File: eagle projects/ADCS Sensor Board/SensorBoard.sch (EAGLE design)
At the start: 113 parts, among them J1 HDR_10_EZFET_DEBUGGER, J3 HDR_2X5_GRPB052VWQS-RC, Q1 PMV16XN, Q2 IRLML6246TRPBF, Q3 IRLML2246TRPBF, U1 MSP430F5529IPN, U2 LMV321, U3 ADS7841E_2K5, U4 LMV321, U5 LMV321, U7 HMC1053, Y1 32.768kHz, Y2 CSTCR4M00G15L99, Y3 32.768kHz

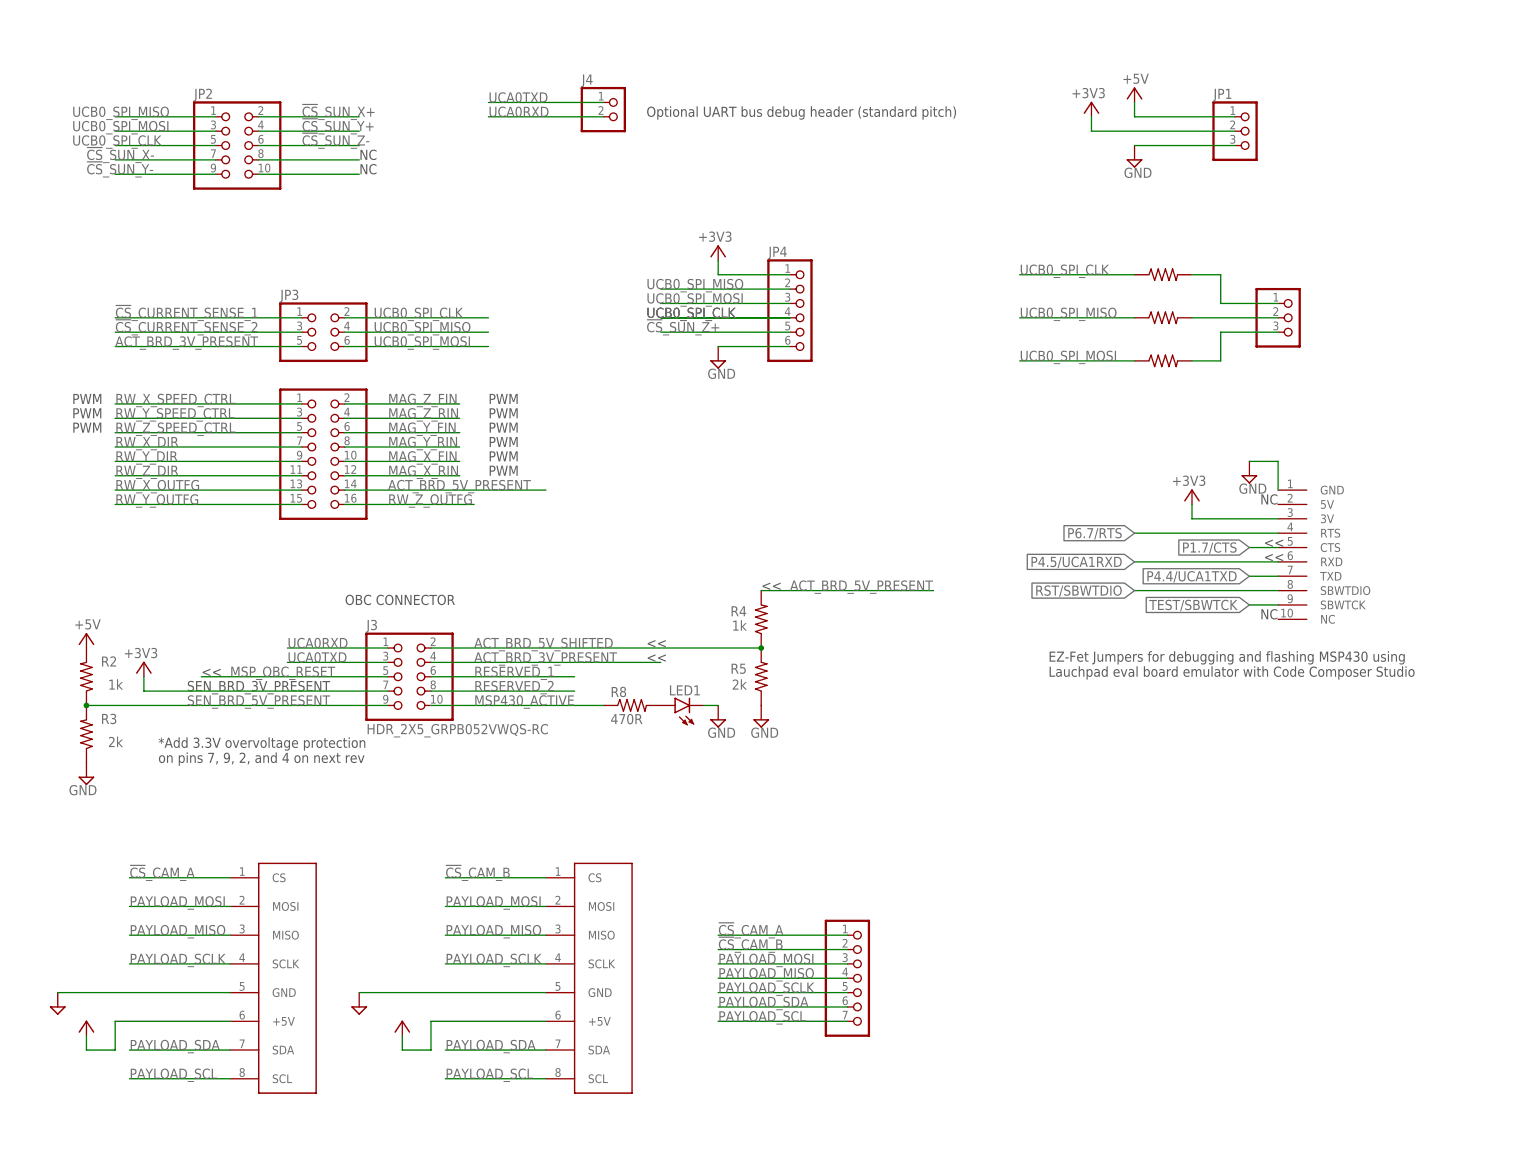
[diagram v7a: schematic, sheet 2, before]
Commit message: tied floating pins on sensor board
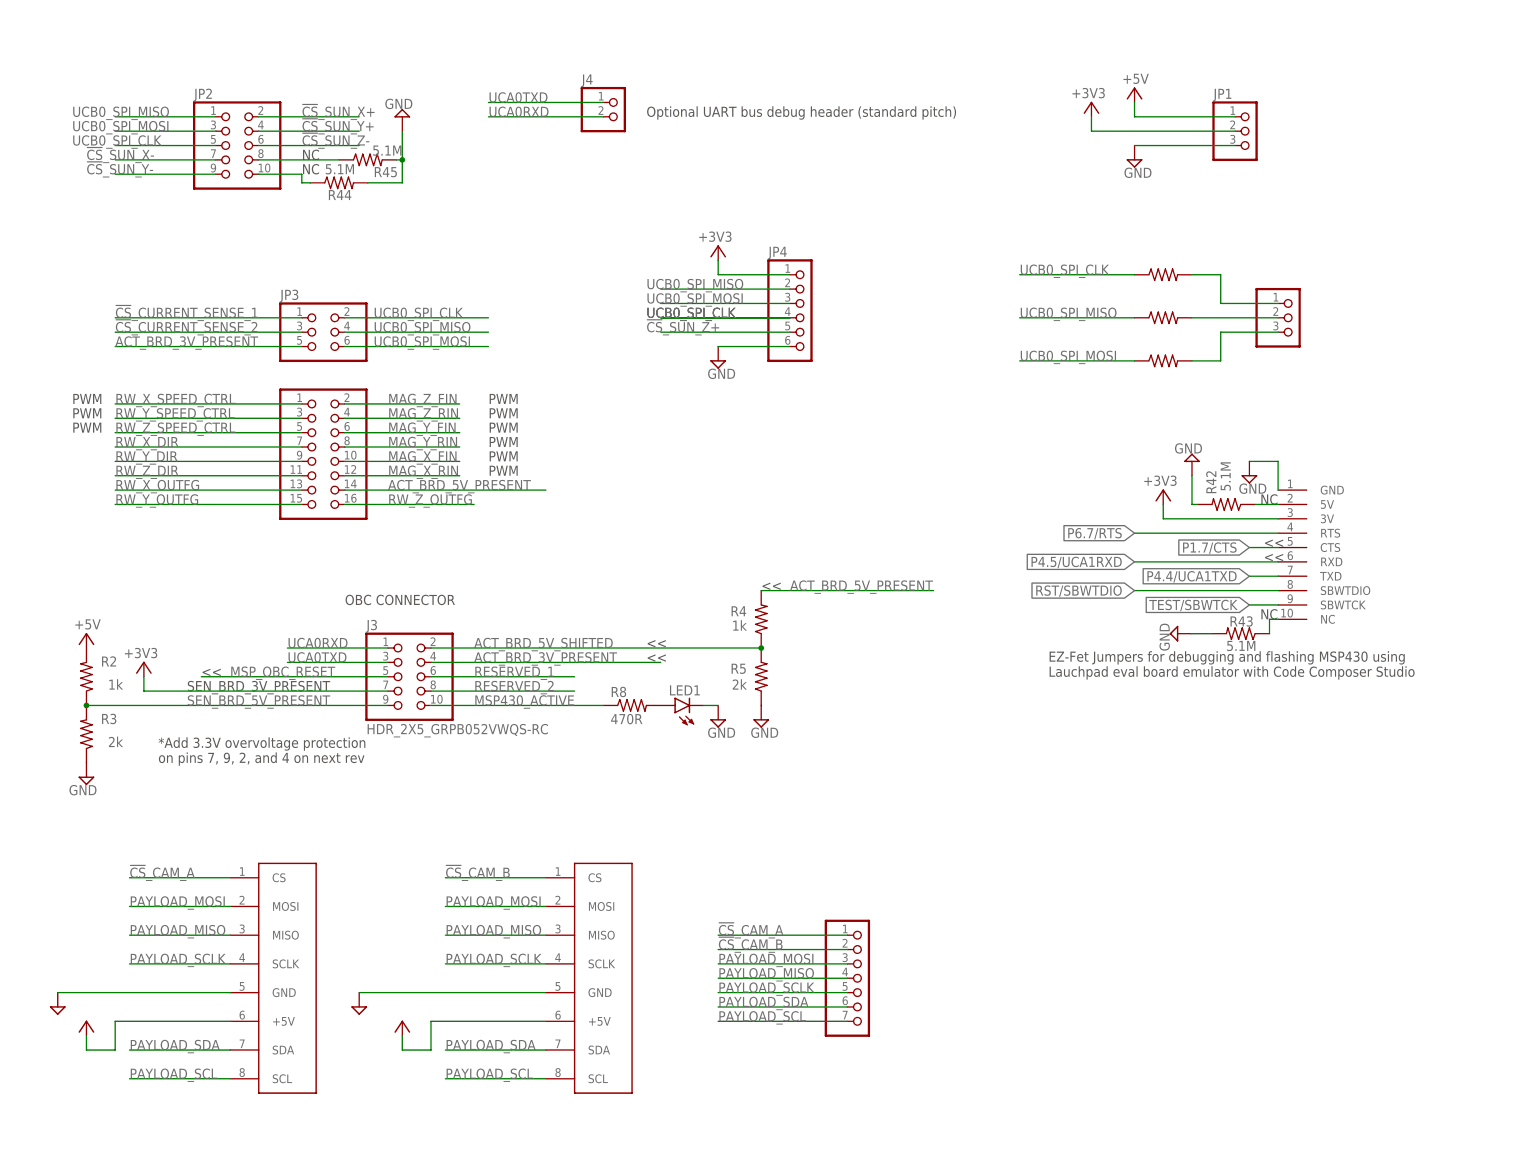
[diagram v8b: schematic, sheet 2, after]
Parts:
- added R38, R42, R43, R44, R45, R46, R47: 5.1M, rcl:R-US_R0402
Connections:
- new net N$30: R38.2, U3.BUSY
- new net N$32: J1.5V, R42.1
- new net N$33: J1.NC, R43.1
- new net N$34: R46.1, U1.V1.8
- new net N$38: R47.1, U1.VUSB
- net GND: now also R38.1, R42.2, R43.2, R44.2, R45.2, R46.2, R47.2
- net N$18: now also R45.1
- net N$19: now also R44.1
